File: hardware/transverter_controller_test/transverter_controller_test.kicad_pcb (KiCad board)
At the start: 2 copper layers, 57 x 42.5 mm, 46 parts, among them J1 USB_C_Receptacle_USB2.0, J2 Conn_01x04_Female, J3 Conn_01x05_Male, J4 Conn_01x05_Male, Q1 Si7141DP, Q2 SI1539CDL-T1-GE3, Q3 Si7141DP, Q4 SI1539CDL-T1-GE3, Q5 Si7141DP, Q6 SI1539CDL-T1-GE3, SW1 SW_Push, U1 MKL26Z64VFT4, U2 MKL02Z32VFG4, U3 INA237, U4 INA237, U5 INA237, U6 24LC64FT-I/MNY, Y1 830108178109

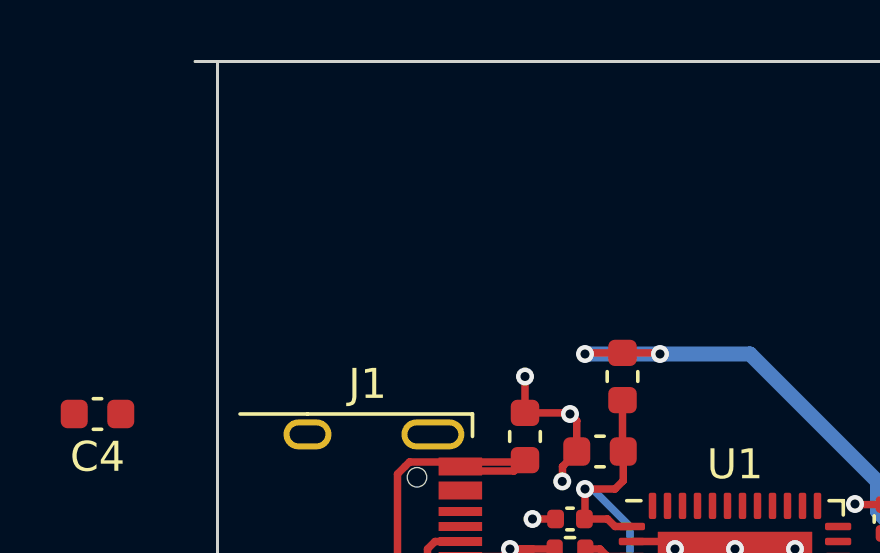
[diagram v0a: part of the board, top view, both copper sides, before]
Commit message: Improved Teensy handling of discovery packets
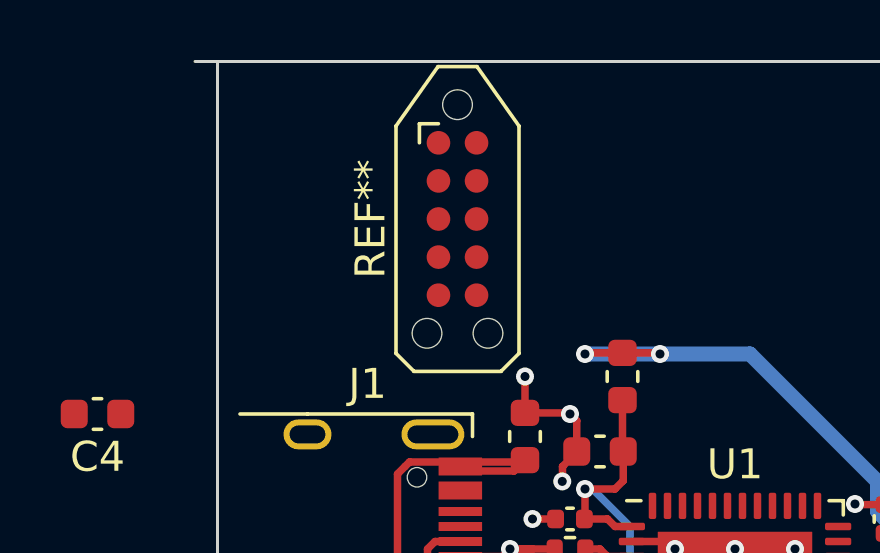
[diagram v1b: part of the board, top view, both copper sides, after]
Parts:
- added REF**: Tag-Connect_TC2050-IDC-NL_2x05_P1.27mm_Vertical, Connector:Tag-Connect_TC2050-IDC-NL_2x05_P1.27mm_Vertical, F.Cu at (93.8, 87.8)
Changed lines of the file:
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@@
     )
+  )
+  (footprint "Connector:Tag-Connect_TC2050-IDC-NL_2x05_P1.27mm_Vertical" (layer "F.Cu")
+    (at 93.75 87.75 -90)
+    (descr "Tag-Connect programming header; http://www.tag-connect.com/Materials/TC2050-IDC-NL%20Datasheet.pdf")
+    (tags "tag connect programming header pogo pins")
+    (attr exclude_from_pos_files exclude_from_bom)
+    (fp_text reference "REF**" (at 0 2.9 90) (layer "F.SilkS")
+      (effects (font (size 1 1) (thickness 0.15)))
+    )
+    (fp_text value "Tag-Connect_TC2050-IDC-NL_2x05_P1.27mm_Vertical" (at 0 4.05 90) (layer "F.Fab")
+      (effects (font (size 1 1) (thickness 0.15)))
+    )
+    (fp_text user "6.35mm Z-KEEPOUT" (at 1 -2.75 90) (layer "Cmts.User")
+      (effects (font (size 0.5 0.5) (thickness 0.125)))
+    )
+    (fp_text user "6.35mm Z-KEEPOUT" (at 1 2.75 90) (layer "Cmts.User")
+      (effects (font (size 0.5 0.5) (thickness 0.125)))
+    )
+    (fp_text user "KEEPOUT" (at 0 0 90) (layer "Cmts.User")
+      (effects (font (size 0.4 0.4) (thickness 0.07)))
+    )
+    (fp_text user "${REFERENCE}" (at 0 0 90) (layer "F.Fab")
+      (effects (font (size 1 1) (thickness 0.15)))
+    )
+    (fp_line (start -5.08 0.65) (end -5.08 -0.65) (layer "F.SilkS") (width 0.12))
+    (fp_line (start -3.175 1.27) (end -3.175 0.635) (layer "F.SilkS") (width 0.12))
+    (fp_line (start 4.48 2.05) (end -3.1 2.05) (layer "F.SilkS") (width 0.12))
+    (fp_line (start -2.54 1.27) (end -3.175 1.27) (layer "F.SilkS") (width 0.12))
+    (fp_line (start -3.1 2.05) (end -5.08 0.65) (layer "F.SilkS") (width 0.12))
+    (fp_line (start 4.48 2.05) (end 5.08 1.45) (layer "F.SilkS") (width 0.12))
+    (fp_line (start 5.08 -1.45) (end 5.08 1.45) (layer "F.SilkS") (width 0.12))
+    (fp_line (start -3.1 -2.05) (end 4.48 -2.05) (layer "F.SilkS") (width 0.12))
+    (fp_line (start -5.08 -0.65) (end -3.1 -2.05) (layer "F.SilkS") (width 0.12))
+    (fp_line (start 4.48 -2.05) (end 5.08 -1.45) (layer "F.SilkS") (width 0.12))
+    (fp_line (start 5.08 -1.45) (end 5.08 1.45) (layer "Dwgs.User") (width 0.1))
+    (fp_line (start 6.223 -2.6) (end 6.223 2.6) (layer "Dwgs.User") (width 0.1))
+    (fp_line (start 2.54 0.635) (end -2.54 0.635) (layer "Dwgs.User") (width 0.1))
+    (fp_line (start 4.2 2.1) (end 5.45 3.35) (layer "Dwgs.User") (width 0.1))
+    (fp_line (start -3.75 -3.15) (end -2.65 -2.05) (layer "Dwgs.User") (width 0.1))
+    (fp_line (start 4.48 2.05) (end 5.08 1.45) (layer "Dwgs.User") (width 0.1))
+    (fp_line (start 1.905 0.635) (end 2.54 0) (layer "Dwgs.User") (width 0.1))
+    (fp_line (start 1.4 -3.35) (end 2.7 -2.05) (layer "Dwgs.User") (width 0.1))
+    (fp_line (start -5.08 -0.65) (end -3.1 -2.05) (layer "Dwgs.User") (width 0.1))
+    (fp_line (start 4.55 -3.35) (end 6.2 -1.7) (layer "Dwgs.User") (width 0.1))
+    (fp_line (start -1.905 0.635) (end -0.635 -0.635) (layer "Dwgs.User") (width 0.1))
+    (fp_line (start -2.1 2.05) (end -0.8 3.35) (layer "Dwgs.User") (width 0.1))
+    (fp_line (start -5.4 -1.9) (end -4.55 -1.05) (layer "Dwgs.User") (width 0.1))
+    (fp_line (start 5.08 -1.45) (end 6.2 -0.33) (layer "Dwgs.User") (width 0.1))
+    (fp_line (start -6.223 -1.4) (end -5.1 -0.277) (layer "Dwgs.User") (width 0.1))
+    (fp_line (start 0.635 0.635) (end 1.905 -0.635) (layer "Dwgs.User") (width 0.1))
+    (fp_line (start 5.1 1.45) (end 6.2 2.55) (layer "Dwgs.User") (width 0.1))
+    (fp_line (start 1.15 2.05) (end 2.45 3.35) (layer "Dwgs.User") (width 0.1))
+    (fp_line (start 2.7 2.05) (end 4 3.35) (layer "Dwgs.User") (width 0.1))
+    (fp_line (start -0.635 0.635) (end 0.635 -0.635) (layer "Dwgs.User") (width 0.1))
+    (fp_line (start -2.54 0) (end -1.905 -0.635) (layer "Dwgs.User") (width 0.1))
+    (fp_line (start -3.45 -3.37) (end 5.453 -3.37) (layer "Dwgs.User") (width 0.1))
+    (fp_line (start 2.54 -0.635) (end 2.54 0.635) (layer "Dwgs.User") (width 0.1))
+    (fp_line (start -1.27 0.635) (end 0 -0.635) (layer "Dwgs.User") (width 0.1))
+    (fp_line (start -6.2 -0.25) (end -2.6 3.35) (layer "Dwgs.User") (width 0.1))
+    (fp_line (start -5.08 0.65) (end -5.08 -0.65) (layer "Dwgs.User") (width 0.1))
+    (fp_line (start 5.1 0.05) (end 6.2 1.15) (layer "Dwgs.User") (width 0.1))
+    (fp_line (start 4.48 2.05) (end -3.1 2.05) (layer "Dwgs.User") (width 0.1))
+    (fp_line (start 5.453 -3.37) (end 6.223 -2.6) (layer "Dwgs.User") (width 0.1))
+    (fp_line (start -2.54 0.635) (end -1.27 -0.635) (layer "Dwgs.User") (width 0.1))
+    (fp_line (start -6.223 1.4) (end -3.45 3.37) (layer "Dwgs.User") (width 0.1))
+    (fp_line (start -0.35 2.1) (end 0.9 3.35) (layer "Dwgs.User") (width 0.1))
+    (fp_line (start -6.223 -1.4) (end -3.45 -3.37) (layer "Dwgs.User") (width 0.1))
+    (fp_line (start 4.4 -2.1) (end 4.45 -2.05) (layer "Dwgs.User") (width 0.1))
+    (fp_line (start 5.453 3.37) (end 6.223 2.6) (layer "Dwgs.User") (width 0.1))
+    (fp_line (start 0 0.635) (end 1.27 -0.635) (layer "Dwgs.User") (width 0.1))
+    (fp_line (start 5.453 3.37) (end -3.45 3.37) (layer "Dwgs.User") (width 0.1))
+    (fp_line (start -3.1 2.05) (end -5.08 0.65) (layer "Dwgs.User") (width 0.1))
+    (fp_line (start 4.48 -2.05) (end 5.08 -1.45) (layer "Dwgs.User") (width 0.1))
+    (fp_line (start 1.27 0.635) (end 2.54 -0.635) (layer "Dwgs.User") (width 0.1))
+    (fp_line (start -3.1 -2.05) (end 4.48 -2.05) (layer "Dwgs.User") (width 0.1))
+    (fp_line (start -2.54 0.635) (end -2.54 -0.635) (layer "Dwgs.User") (width 0.1))
+    (fp_line (start -4.6 -2.5) (end -3.75 -1.65) (layer "Dwgs.User") (width 0.1))
+    (fp_line (start -6.2 0.6) (end -3.45 3.35) (layer "Dwgs.User") (width 0.1))
+    (fp_line (start -2.15 -3.35) (end -0.85 -2.05) (layer "Dwgs.User") (width 0.1))
+    (fp_line (start -0.5 -3.35) (end 0.8 -2.05) (layer "Dwgs.User") (width 0.1))
+    (fp_line (start -6.223 1.4) (end -6.223 -1.4) (layer "Dwgs.User") (width 0.1))
+    (fp_line (start -2.54 -0.635) (end 2.54 -0.635) (layer "Dwgs.User") (width 0.1))
+    (fp_line (start 3.15 -3.35) (end 4.4 -2.1) (layer "Dwgs.User") (width 0.1))
+    (fp_line (start 4.63 2.3) (end -3.19 2.3) (layer "F.CrtYd") (width 0.05))
+    (fp_line (start 5.33 -1.6) (end 5.33 1.6) (layer "F.CrtYd") (width 0.05))
+    (fp_line (start 4.63 -2.3) (end 5.33 -1.6) (layer "F.CrtYd") (width 0.05))
+    (fp_line (start -5.33 -0.77) (end -3.19 -2.3) (layer "F.CrtYd") (width 0.05))
+    (fp_line (start -5.33 0.77) (end -5.33 -0.77) (layer "F.CrtYd") (width 0.05))
+    (fp_line (start 4.63 2.3) (end 5.33 1.6) (layer "F.CrtYd") (width 0.05))
+    (fp_line (start -3.19 2.3) (end -5.33 0.77) (layer "F.CrtYd") (width 0.05))
+    (fp_line (start -3.19 -2.3) (end 4.63 -2.3) (layer "F.CrtYd") (width 0.05))
+    (pad "" np_thru_hole circle locked (at 3.81 1.016 270) (size 0.9906 0.9906) (drill 0.9906) (layers *.Cu *.Mask))
+    (pad "" np_thru_hole circle locked (at -3.81 0 270) (size 0.9906 0.9906) (drill 0.9906) (layers *.Cu *.Mask))
+    (pad "" np_thru_hole circle locked (at 3.81 -1.016 270) (size 0.9906 0.9906) (drill 0.9906) (layers *.Cu *.Mask))
+    (pad "1" connect circle locked (at -2.54 0.635 270) (size 0.7874 0.7874) (layers "F.Cu" "F.Mask"))
+    (pad "2" connect circle locked (at -1.27 0.635 270) (size 0.7874 0.7874) (layers "F.Cu" "F.Mask"))
+    (pad "3" connect circle locked (at 0 0.635 270) (size 0.7874 0.7874) (layers "F.Cu" "F.Mask"))
+    (pad "4" connect circle locked (at 1.27 0.635 270) (size 0.7874 0.7874) (layers "F.Cu" "F.Mask"))
+    (pad "5" connect circle locked (at 2.54 0.635 270) (size 0.7874 0.7874) (layers "F.Cu" "F.Mask"))
+    (pad "6" connect circle locked (at 2.54 -0.635 270) (size 0.7874 0.7874) (layers "F.Cu" "F.Mask"))
+    (pad "7" connect circle locked (at 1.27 -0.635 270) (size 0.7874 0.7874) (layers "F.Cu" "F.Mask"))
+    (pad "8" connect circle locked (at 0 -0.635 270) (size 0.7874 0.7874) (layers "F.Cu" "F.Mask"))
+    (pad "9" connect circle locked (at -1.27 -0.635 270) (size 0.7874 0.7874) (layers "F.Cu" "F.Mask"))
+    (pad "10" connect circle locked (at -2.54 -0.635 270) (size 0.7874 0.7874) (layers "F.Cu" "F.Mask"))
   )
   (footprint "Resistor_SMD:R_2512_6332Metric" (layer "F.Cu")

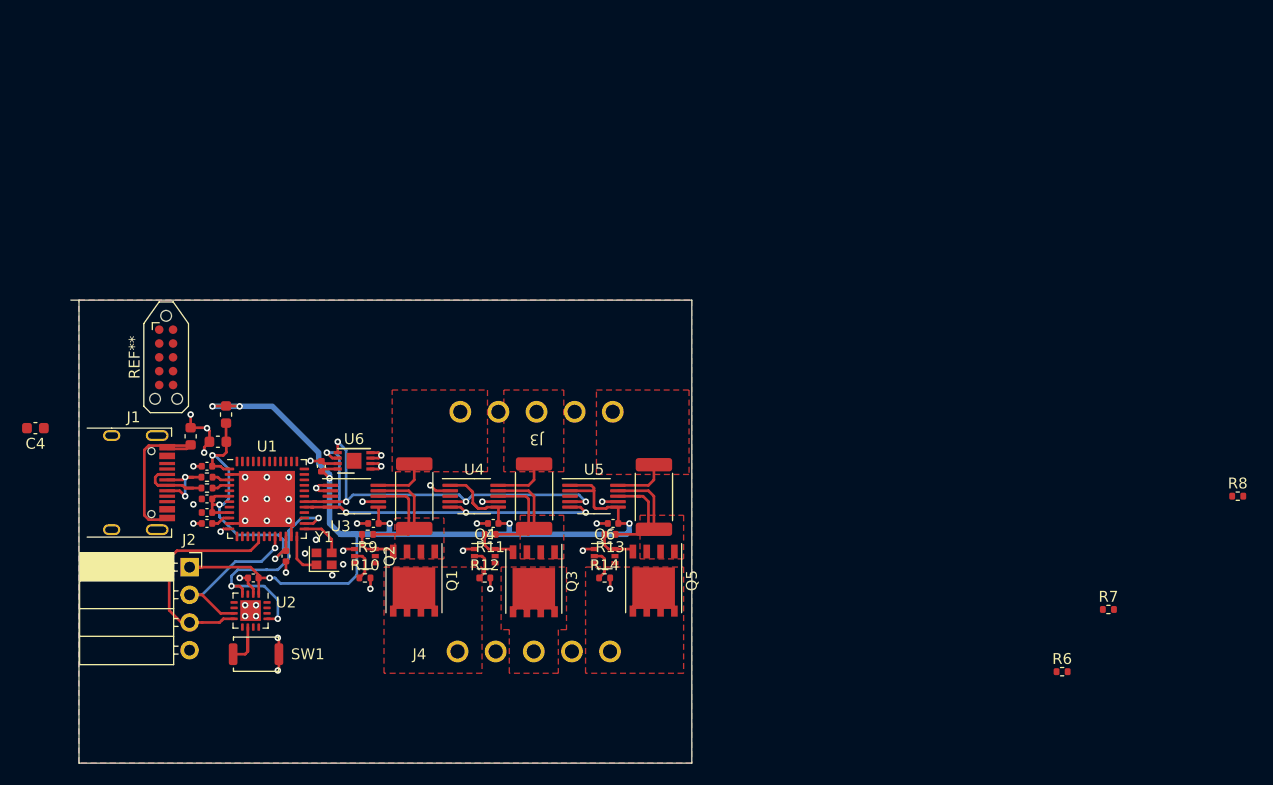
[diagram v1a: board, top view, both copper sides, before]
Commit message: v1 transverter interface complete
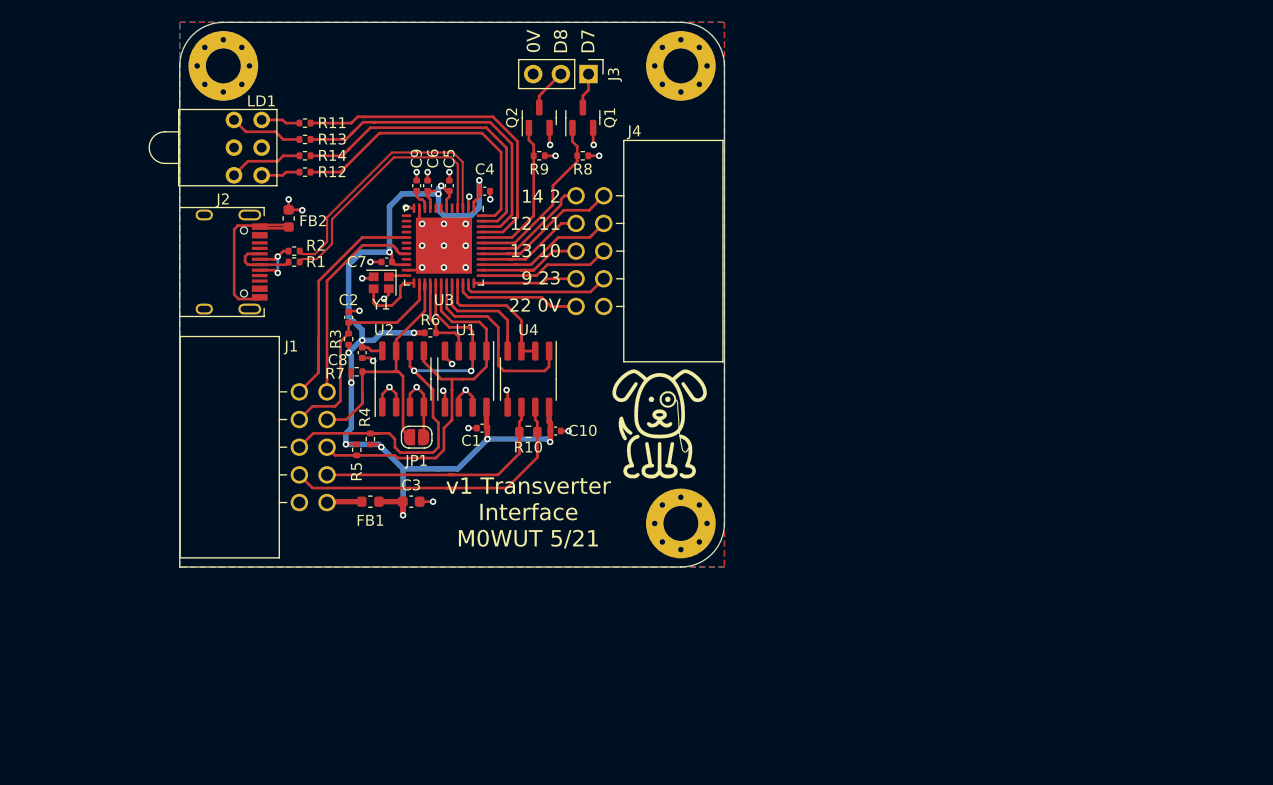
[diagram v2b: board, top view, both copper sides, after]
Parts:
- removed C11, C12: 100n, Capacitor_SMD:C_0402_1005Metric
- removed Q3, Q5: Si7141DP, Package_SO:PowerPAK_SO-8_Single
- removed Q4, Q6: SI1539CDL-T1-GE3, Package_TO_SOT_SMD:SOT-363_SC-70-6
- removed REF**: Tag-Connect_TC2050-IDC-NL_2x05_P1.27mm_Vertical, Connector:Tag-Connect_TC2050-IDC-NL_2x05_P1.27mm_Vertical
- removed SW1: SW_Push, Button_Switch_SMD:SW_Push_SPST_NO_Alps_SKRK
- removed U5: INA237, Package_SO:VSSOP-10_3x3mm_P0.5mm
- removed U6: 24LC64FT-I/MNY, Package_DFN_QFN:DFN-8-1EP_3x2mm_P0.5mm_EP1.36x1.46mm
- added H1: MountingHole_Pad, MountingHole:MountingHole_3.2mm_M3_Pad_Via, F.Cu at (99.0, 61.0)
- added H2: MountingHole_Pad, MountingHole:MountingHole_3.2mm_M3_Pad_Via, F.Cu at (141.0, 103.0)
- added H3: MountingHole_Pad, MountingHole:MountingHole_3.2mm_M3_Pad_Via, F.Cu at (141.0, 61.0)
- added JP1: SolderJumper_2_Open, Jumper:SolderJumper-2_P1.3mm_Open_RoundedPad1.0x1.5mm, F.Cu at (116.8, 95.1)
- added LD1: Kingbright_WP130WCP_2EGW, LED_WUT:Kingbright_WP130WCP_2EGW, F.Cu at (102.5, 68.5)
- added M1: Logo_10mmx10mm, Misc_WUT:Logo_10mmx10mm, F.Cu at (139.0, 94.0)
- C1: value 10u -> 100n; footprint Capacitor_SMD:C_0603_1608Metric -> Capacitor_SMD:C_0402_1005Metric
- C2: value 100n -> DNF
- C3: value 100n -> 10u; footprint Capacitor_SMD:C_0402_1005Metric -> Capacitor_SMD:C_0603_1608Metric
- C4: value DNF -> 100n; footprint Capacitor_SMD:C_0603_1608Metric -> Capacitor_SMD:C_0402_1005Metric
- J1: value USB_C_Receptacle_USB2.0 -> CNC Tech 3020-10-0200-00‎; footprint Connector_WUT:USB-C_HRO_TYPE-C-31-M-12 -> Connector_WUT:Header_CNC-Tech_3020-10-0200-00_2x5_TH_RA
- J2: value Conn_01x04_Female -> USB_C_Receptacle_USB2.0; footprint Connector_PinSocket_2.54mm:PinSocket_1x04_P2.54mm_Horizontal -> Connector_WUT:USB-C_HRO_TYPE-C-31-M-12
- J3: value Conn_01x05_Male -> Conn_01x03_Male; footprint Connector_WUT:Weidmuller_SL3.5-5-90G -> Connector_PinHeader_2.54mm:PinHeader_1x03_P2.54mm_Vertical
- J4: value Conn_01x05_Male -> CNC Tech 3020-10-0200-00‎; footprint Connector_WUT:Weidmuller_SL3.5-5-90G -> Connector_WUT:Header_CNC-Tech_3020-10-0200-00_2x5_TH_RA
- Q1: value Si7141DP -> DMN62D0U-13; footprint Package_SO:PowerPAK_SO-8_Single -> Package_TO_SOT_SMD:SOT-23
- Q2: value SI1539CDL-T1-GE3 -> DMN62D0U-13; footprint Package_TO_SOT_SMD:SOT-363_SC-70-6 -> Package_TO_SOT_SMD:SOT-23
- R10: value 10k -> DNF; footprint Resistor_SMD:R_0402_1005Metric -> Resistor_SMD:R_0603_1608Metric
- R11, R12, R13, R14, R7: value 10k -> 1k
- R3: value 0R1 -> 10k; footprint Resistor_SMD:R_2512_6332Metric -> Resistor_SMD:R_0402_1005Metric
- R4, R5: value 0R1 -> 4k7; footprint Resistor_SMD:R_2512_6332Metric -> Resistor_SMD:R_0402_1005Metric
- U1: value MKL26Z64VFT4 -> PCT2075D; footprint Package_DFN_QFN:QFN-48-1EP_7x7mm_P0.5mm_EP5.15x5.15mm -> Package_SO:SO-8_3.9x4.9mm_P1.27mm
- U2: value MKL02Z32VFG4 -> 24LC024-I/SN; footprint Package_DFN_QFN:QFN-16-1EP_3x3mm_P0.5mm_EP1.9x1.9mm -> Package_SO:SO-8_3.9x4.9mm_P1.27mm
- U3: value INA237 -> MKL26Z64VFT4; footprint Package_SO:VSSOP-10_3x3mm_P0.5mm -> Package_DFN_QFN:QFN-48-1EP_7x7mm_P0.5mm_EP5.15x5.15mm
- U4: value INA237 -> MAX3483ESA+; footprint Package_SO:VSSOP-10_3x3mm_P0.5mm -> Package_SO:SO-8_3.9x4.9mm_P1.27mm
- moved R7 72.4 mm to (111.2, 89.1)
- moved R8 67.8 mm to (132.0, 69.2)
- moved R6 65.8 mm to (118.0, 85.5)
- moved R14 47.5 mm to (106.5, 69.2), turned to 180 degrees
- moved C4 46.6 mm to (123.0, 72.5), turned to 0 degrees
- moved R13 45.8 mm to (106.5, 67.8)
- moved Q1 45.2 mm to (132.0, 65.8), turned to 90 degrees
- moved Q2 43.3 mm to (128.0, 65.8), turned to 90 degrees
- moved R11 41.4 mm to (106.5, 66.2)
- moved R12 40.7 mm to (106.5, 70.8), turned to 180 degrees
- moved R9 38.2 mm to (128.0, 69.2), turned to 0 degrees
- moved C5 37.4 mm to (119.8, 72.0), turned to 90 degrees
- moved J4 37.0 mm to (131.4, 78.0), turned to 90 degrees
- moved C6 36.4 mm to (117.8, 72.0), turned to 90 degrees
- moved J3 31.4 mm to (132.5, 61.8), turned to -90 degrees
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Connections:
- C1 pad 1: Net-(C1-Pad1) -> +3V3
- C2 pad 1: Net-(C1-Pad1) -> /RESET_B
- C3 pad 1: Net-(C1-Pad1) -> +3V3
- C4 pad 1: Net-(C4-Pad1) -> +3V3
- C5 pad 1: Net-(C1-Pad1) -> +3V3
- C6 pad 1: Net-(C1-Pad1) -> +3V3
- C7 pad 1: Net-(C7-Pad1) -> +3V3
- C9 pad 1: +3V3 -> Net-(C9-Pad1)
- FB1 pad 1: Net-(FB1-Pad1) -> +3V3
- FB1 pad 2: GND -> Net-(FB1-Pad2)
- FB2 pad 1: +3V3 -> Net-(FB2-Pad1)
- FB2 pad 2: Net-(C1-Pad1) -> GND
- J3 pad 1: +48V -> Net-(J3-Pad1)
- J3 pad 2: GND -> Net-(J3-Pad2)
- J3 pad 3: +28V -> GND
- J4 pad 1: Net-(J4-Pad1) -> /SPARE_1
- J4 pad 2: GND -> /SPARE_2
- J4 pad 3: Net-(J4-Pad3) -> /SPARE_3
- J4 pad 4: GND -> /SPARE_4
- J4 pad 5: Net-(J4-Pad5) -> /SPARE_5
- Q1 pad 2: Net-(Q1-Pad1) -> GND
- Q1 pad 3: Net-(Q1-Pad1) -> Net-(J3-Pad1)
- Q2 pad 1: GND -> Net-(Q2-Pad1)
- Q2 pad 2: Net-(Q2-Pad2) -> GND
- Q2 pad 3: unconnected-(Q2-Pad3) -> Net-(J3-Pad2)
- R1 pad 1: Net-(J1-PadA6) -> Net-(J2-PadA7)
- R1 pad 2: Net-(R1-Pad2) -> /D_P
- R10 pad 1: Net-(Q2-Pad2) -> /RS485_B
- R10 pad 2: GND -> /RS485_A
- R11 pad 1: Net-(Q3-Pad1) -> /LED_TX
- R12 pad 1: Net-(Q4-Pad2) -> /LED_RX
- R12 pad 2: GND -> Net-(LD1-Pad3)
- R13 pad 1: Net-(Q5-Pad1) -> /LED_ERROR
- R14 pad 1: Net-(Q6-Pad2) -> /LED_STATUS
- R14 pad 2: GND -> Net-(LD1-Pad6)
- R2 pad 1: Net-(J1-PadA7) -> Net-(J2-PadA6)
- R2 pad 2: Net-(R2-Pad2) -> /D_N
- R3 pad 1: +12V -> +3V3
- R3 pad 2: Net-(Q1-Pad1) -> /RESET_B
- R4 pad 1: +28V -> +3V3
- R4 pad 2: Net-(Q3-Pad1) -> /SCL
- R5 pad 1: +48V -> +3V3
- R5 pad 2: Net-(Q5-Pad1) -> /SDA
- R6 pad 2: /~12V_ALERT -> /~OVERTEMP
- R7 pad 2: /~28V_ALERT -> /WP
- R8 pad 1: +3V3 -> Net-(Q1-Pad1)
- R8 pad 2: /~12V_ALERT -> GND
- R9 pad 1: Net-(Q1-Pad1) -> Net-(Q2-Pad1)
- R9 pad 2: Net-(Q1-Pad4) -> GND
- U1 pad 1: Net-(C1-Pad1) -> /SDA
- U1 pad 2: GND -> /SCL
- U1 pad 3: Net-(R1-Pad2) -> /~OVERTEMP
- U1 pad 4: Net-(R2-Pad2) -> GND
- U1 pad 5: Net-(C4-Pad1) -> GND
- U1 pad 6: Net-(C1-Pad1) -> GND
- U1 pad 7: unconnected-(U1-Pad7) -> GND
- U1 pad 8: unconnected-(U1-Pad8) -> +3V3
- U2 pad 1: +3V3 -> GND
- U2 pad 3: unconnected-(U2-Pad3) -> GND
- U2 pad 4: /RESET_B -> GND
- U2 pad 5: unconnected-(U2-Pad5) -> /SDA
- U2 pad 6: unconnected-(U2-Pad6) -> /SCL
- U2 pad 7: /PTA3 -> /WP
- U2 pad 8: /PTA0 -> +3V3
- U3 pad 1: GND -> +3V3
- U3 pad 10: +12V -> Net-(C9-Pad1)
- U3 pad 3: /~12V_ALERT -> /D_N
- U3 pad 4: /SDA -> /D_P
- U3 pad 5: /SCL -> unconnected-(U3-Pad5)
- U3 pad 7: GND -> unconnected-(U3-Pad7)
- U3 pad 8: Net-(Q1-Pad1) -> unconnected-(U3-Pad8)
- U3 pad 9: Net-(Q1-Pad1) -> +3V3
- U4 pad 1: +3V3 -> /RX
- U4 pad 2: GND -> /~R~/W
- U4 pad 3: /~28V_ALERT -> /~R~/W
- U4 pad 4: /SDA -> /TX
- U4 pad 5: /SCL -> GND
- U4 pad 6: +3V3 -> /RS485_A
- U4 pad 7: GND -> /RS485_B
- U4 pad 8: Net-(Q3-Pad1) -> +3V3
- Y1 pad 1: Net-(U1-Pad24) -> Net-(U3-Pad24)
- Y1 pad 3: Net-(U1-Pad25) -> Net-(U3-Pad25)
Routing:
- net /LED_TX: track 0.00 -> 31.4 mm
- net /LED_ERROR: track 0.00 -> 30.7 mm
- net Net-(C1-Pad1): track 30.4 -> 0.00 mm, vias 3 -> 0
- net /RS485_B: track 0.00 -> 29.0 mm
- net /LED_STATUS: track 0.00 -> 28.6 mm
- net /WP: track 0.00 -> 28.4 mm
- net /LED_RX: track 0.00 -> 27.2 mm
- net /D_N: track 0.00 -> 24.9 mm
- net /D_P: track 0.00 -> 24.2 mm
- net /RS485_A: track 0.00 -> 24.0 mm
- net /RX: track 0.00 -> 17.9 mm
- net Net-(FB2-Pad1): track 0.00 -> 16.5 mm
- net Net-(Q5-Pad1): track 16.2 -> 0.00 mm
- net Net-(Q3-Pad1): track 16.0 -> 0.00 mm
- net Net-(FB1-Pad1): track 15.0 -> 0.00 mm
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- removed copper zone on F.Cu, net +12V
- removed copper zone on F.Cu, net +28V
- removed copper zone on F.Cu, net +48V
- removed copper zone on F.Cu, net Net-(J4-Pad1)
- removed copper zone on F.Cu, net Net-(J4-Pad3)
- removed copper zone on F.Cu, net Net-(J4-Pad5)
- removed copper zone on F.Cu, net Net-(Q1-Pad1)
- removed copper zone on F.Cu, net Net-(Q3-Pad1)
- removed copper zone on F.Cu, net Net-(Q5-Pad1)
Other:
- board size 57 x 42.5 mm -> 50 x 50 mm
- board text added: "0V"
- board text added: "12 11"
- board text added: "13 10"
- board text added: "14 2"
- board text added: "22 0V"
- board text added: "9 23"
- board text added: "D7"
- board text added: "D8"
- board text added: "v1 Transverter Interface M0WUT 5/21"
